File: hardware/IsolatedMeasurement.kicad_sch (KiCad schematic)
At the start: 27 parts, among them IC10 REF196GSZ-REEL, IC4 MCP3561T-E_NC, IC5 ADUM7440ARQZ, P2 AM1LS-0505S-NZ, U3 >

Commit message: board sync and measurments section adjustments
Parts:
- C46: value 1nF -> 100nF
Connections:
- net HV_+3.3V: now also C46.1, IC10.2 (VSS), IC10.3 (~{SLEEP})
- net HV_+5V: no longer names the net of C56.1, C58.2, P2.5 (VOUT+), R12.2, U3.3 (VI)
- net HV_+5V: no longer C46.1, IC10.2 (VSS), IC10.3 (~{SLEEP})
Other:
- note added: "3V REF"
- note added: "Minimal current - 20mA R12 - additional load resistor to cap the current draw"
- note removed: "Minimal current - 20mA R - additional load resistor to cap the current draw"
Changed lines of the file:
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@@
     (stroke (width 0) (type default) (color 0 0 0 0))
   )
-  (text "Minimal current - 20mA\nR - additional load resistor to cap\nthe current draw"
+  (text "Minimal current - 20mA\nR12 - additional load resistor to cap\nthe current draw"
     (at 243.84 50.165 0)
     (effects (font (size 1.27 1.27)) (justify left bottom))
@@
     (effects (font (size 1.27 1.27)) (justify left bottom))
   )
+  (text "3V REF\n" (at 122.555 135.89 0)
+    (effects (font (size 3 3) (thickness 1) bold) (justify left bottom))
+  )
   (text "SPI iso\n" (at 214.63 111.125 0)
     (effects (font (size 5 5) (thickness 1) bold) (justify left bottom))
@@
     (effects (font (size 1.27 1.27)) (justify right bottom))
   )
-  (label "HV_+5V" (at 233.045 62.865 90)
-    (effects (font (size 1.27 1.27)) (justify left bottom))
-  )
   (label "3.3V_REF" (at 60.325 134.62 180)
     (effects (font (size 1.27 1.27)) (justify right bottom))
@@
     (effects (font (size 1.27 1.27)) (justify left bottom))
   )
+  (label "HV_+3.3V" (at 116.205 142.24 90)
+    (effects (font (size 1.27 1.27)) (justify left bottom))
+  )
   (label "HV_+3.3V" (at 264.795 65.405 0)
     (effects (font (size 1.27 1.27)) (justify left bottom))
@@
   )
   (label "SDO" (at 149.86 52.705 0)
-    (effects (font (size 1.27 1.27)) (justify left bottom))
-  )
-  (label "HV_+5V" (at 116.205 142.24 90)
     (effects (font (size 1.27 1.27)) (justify left bottom))
   )
@@
       (effects (font (size 1.27 1.27)) (justify left))
     )
-    (property "Value" "1nF" (id 1) (at 111.125 157.48 90)
-      (effects (font (size 1.27 1.27)) (justify left))
-    )
+    (property "Value" "100nF" (id 1) (at 111.125 157.48 90)
+      (effects (font (size 1.27 1.27)) (justify left))
+    )

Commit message: measurments section changes, sorted components on the board into groups, changed main connector and added seprate for AIRs, added IMD PWM input as well as AIR fault detection
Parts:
- removed U3: >, symbol Regulator_Linear:LM1117-3.3
- added IC11: AP7365-33YRG-13, AP736533YRG13, symbol AP7365-33YRG-13:AP7365-33YRG-13
- C58, C59: value 1uF -> 100nF
- IC10: value REF196GSZ-REEL -> REF193GSZ-REEL
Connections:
- net HV_+3.3V: now also IC11.3 (VO)
- net HV_IN-: now also IC11.1 (GND)
- net V_HV+: now also IC4.4 (CH1); no longer IC4.3 (CH0)
- net V_HV-: now also IC4.3 (CH0); no longer IC4.4 (CH1)
- net at C56.1, C58.2, P2.5 (VOUT+)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: now also IC11.2 (VI)
- net 3.3V_REF renamed 3V_REF
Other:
- note added: "Minimal current - 20mA R - additional load resistor to cap the current draw"
- note added: "V_HV_REF- can be adjusted, default is HV_GND WARNING! USES REF_V! that means high resistance & precision resistors should be used"
- note added: "V_{inmax} = 2,2k / (2,2 k + 4 x 200k) * 600 = ~1,65V I_{max} = 600V / 802,2kOhm = ~0,000747A P_{max} = 0,000747A * 600V = 0,4482W P_{max1R} = 0,000747A * 598,35V = 0,44696745W P_{max4R} = 0,000747A * P_{max1R} / 4 = 0,1117418625W P_{maxR} = ~0,25W????"
- note removed: "Minimal current - 20mA R12 - additional load resistor to cap the current draw"
- note removed: "V_HV_REF- can be adjusted, default is HV_GND"
- note removed: "V_{inmax} = 2,2k / (2,2 k + 4 x 200k) * 600 = ~1,65V I_{max} = 600V / 802,2kOhm = ~0,000747A P_{max} = 0,000747A * 600V = 0,4482W P_{max1R} = 0,000747A * 598,35V = 0,44696745W P_{max4R} = 0,000747A * P_{max1R} / 4 = 0,1117418625W P_{maxR} = ~0,25W???? (i guess)"
- moved on the sheet: R25, R26

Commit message: changed few connectors, finished board HV section and other minor changes
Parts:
- renumbered C23 to C13, C26 to C14, C31 to C17, C32 to C18, C33 to C19, C47 to C20, C49 to C36, C56 to C37, C58 to C38, C59 to C39, C22 to C7, C46 to C9, IC4 to IC2, IC5 to IC3, IC11 to IC6, IC10 to IC9, L7 to L2, L6 to L5, P2 to P1, R2 to R1, R12 to R11, R25 to R20, R26 to R21, R4 to R3, R6 to R5, R8 to R7, R10 to R9
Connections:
- net SCK: now also IC3.13 (VOB); no longer IC2.12 (SCK), IC3.12 (VOC), IC3.5 (VIC)
- net SDI: now also IC3.12 (VOC); no longer IC2.13 (SDI), IC3.13 (VOB), IC3.4 (VIB)
- net SDO: now also IC3.11 (VOD); no longer IC2.14 (SDO), IC3.14 (VOA), IC3.3 (VIA)
- net ~{CS}: now also IC3.14 (VOA); no longer IC2.11 (~{CS}), IC3.11 (VOD), IC3.6 (VID)
- new net HV_SCK: IC2.12 (SCK), IC3.4 (VIB)
- new net HV_SDI: IC2.13 (SDI), IC3.5 (VIC)
- new net HV_SDO: IC2.14 (SDO), IC3.6 (VID)
- new net HV_~{CS}: IC2.11 (~{CS}), IC3.3 (VIA)

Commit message: board sync
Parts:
- R10: renamed from R9; value 2,2k -> 4k; footprint Resistor_SMD:R_0603_1608Metric -> Resistor_SMD:R_1206_3216Metric
- R2: renamed from R1; footprint Resistor_SMD:R_0603_1608Metric -> Resistor_SMD:R_1206_3216Metric; Mouser Part Number (none) -> 754-RGV3216P-2003BT1
- R4: renamed from R3; footprint Resistor_SMD:R_0603_1608Metric -> Resistor_SMD:R_1206_3216Metric; Mouser Part Number (none) -> 754-RGV3216P-2003BT1
- R6: renamed from R5; footprint Resistor_SMD:R_0603_1608Metric -> Resistor_SMD:R_1206_3216Metric; Mouser Part Number (none) -> 754-RGV3216P-2003BT1
- R8: renamed from R7; footprint Resistor_SMD:R_0603_1608Metric -> Resistor_SMD:R_1206_3216Metric; Mouser Part Number (none) -> 754-RGV3216P-2003BT1
- renumbered C7 to C22, C13 to C23, C14 to C26, C17 to C31, C18 to C32, C19 to C33, C9 to C46, C20 to C47, C36 to C49, C37 to C56, C38 to C58, C39 to C59, IC9 to IC10, IC6 to IC11, IC2 to IC4, IC3 to IC5, L5 to L6, L2 to L7, P1 to P2, R11 to R12, R20 to R25, R21 to R26
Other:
- note added: "V_{max_mes} = 3V 3V = 588V * x / ( 800 000 + x ) 585x = 2'400'000 x = 4102,56 Ohm R = 4kOhm"
- note removed: "V_{inmax} = 2,2k / (2,2 k + 4 x 200k) * 600 = ~1,65V I_{max} = 600V / 802,2kOhm = ~0,000747A P_{max} = 0,000747A * 600V = 0,4482W P_{max1R} = 0,000747A * 598,35V = 0,44696745W P_{max4R} = 0,000747A * P_{max1R} / 4 = 0,1117418625W P_{maxR} = ~0,25W????"

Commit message: remake in progress
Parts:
- renumbered C23 to C13, C26 to C14, C31 to C17, C32 to C18, C33 to C19, C47 to C20, C49 to C36, C56 to C37, C58 to C38, C59 to C39, C22 to C7, C46 to C9, IC4 to IC2, IC5 to IC3, IC11 to IC6, IC10 to IC9, L7 to L2, L6 to L5, P2 to P1, R2 to R1, R12 to R11, R25 to R20, R26 to R21, R4 to R3, R6 to R5, R8 to R7, R10 to R9

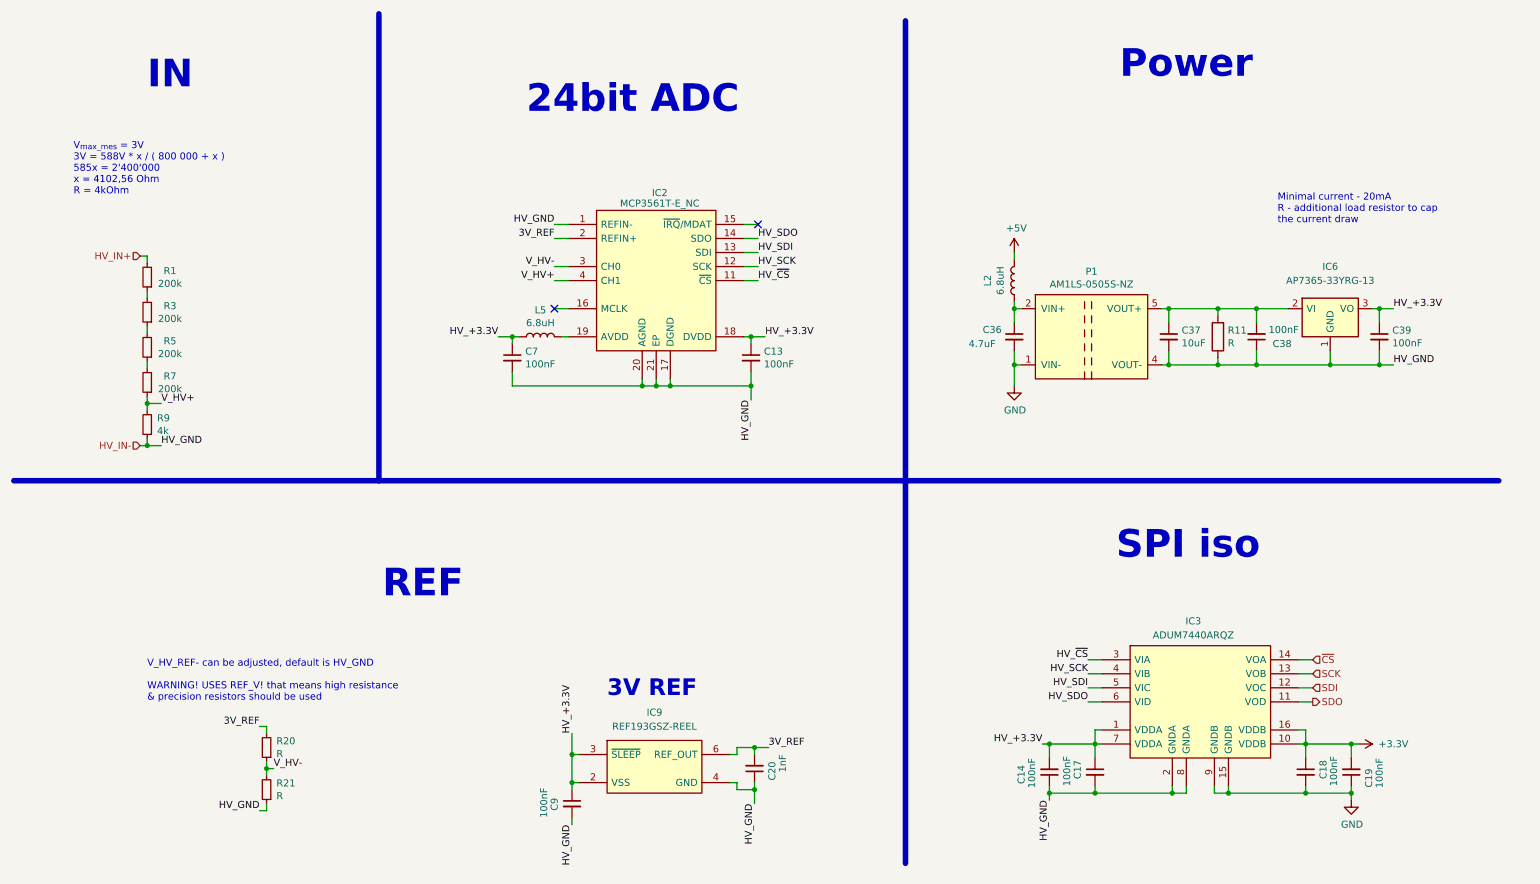
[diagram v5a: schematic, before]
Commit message: major changes: conn, fans, inputs and others
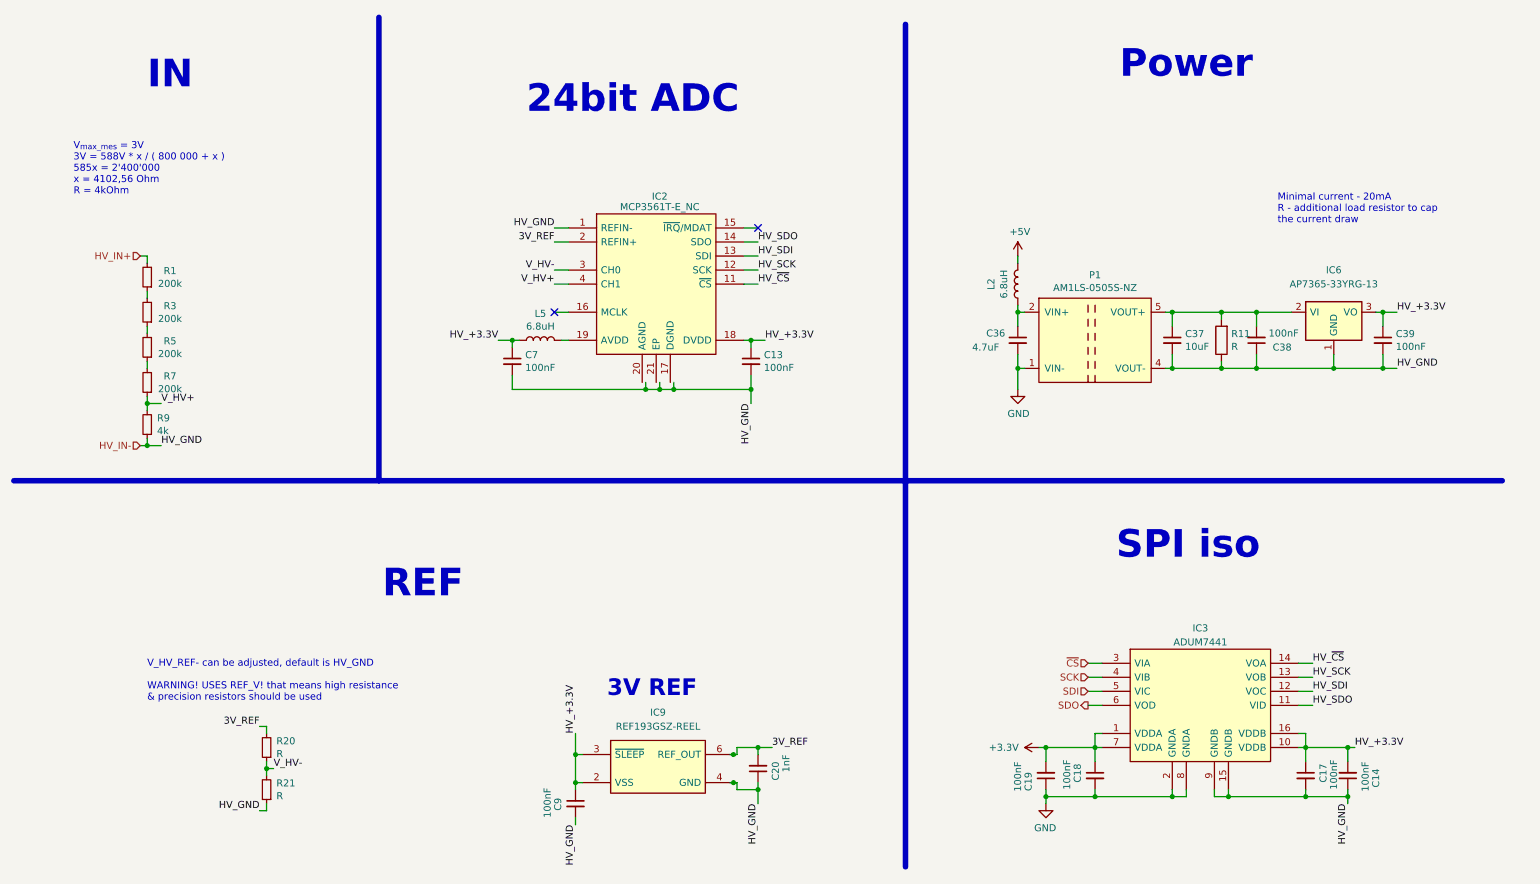
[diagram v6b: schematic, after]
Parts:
- IC3: value ADUM7440ARQZ -> ADUM7441
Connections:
- net +3V3: now also IC3.1 (VDDA), IC3.7 (VDDA); no longer IC3.10 (VDDB), IC3.16 (VDDB)
- net GND: now also IC3.2 (GNDA), IC3.8 (GNDA); no longer IC3.15 (GNDB), IC3.9 (GNDB)
- net HV_+3.3V: now also IC3.10 (VDDB), IC3.16 (VDDB); no longer IC3.1 (VDDA), IC3.7 (VDDA)
- net HV_IN-: now also IC3.15 (GNDB), IC3.9 (GNDB); no longer IC2.17 (DGND), IC2.20 (AGND), IC2.21 (EP), IC3.2 (GNDA), IC3.8 (GNDA)
- net HV_SCK: now also IC3.13 (VOB); no longer IC3.4 (VIB)
- net HV_SDI: now also IC3.12 (VOC); no longer IC3.5 (VIC)
- net HV_SDO: now also IC3.11 (VID); no longer IC3.6 (VID)
- net HV_~{CS}: now also IC3.14 (VOA); no longer IC3.3 (VIA)
- net SCK: now also IC3.4 (VIB); no longer IC3.13 (VOB)
- net SDI: now also IC3.5 (VIC); no longer IC3.12 (VOC)
- net SDO: now also IC3.6 (VOD); no longer IC3.11 (VOD)
- net ~{CS}: now also IC3.3 (VIA); no longer IC3.14 (VOA)
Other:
- moved on the sheet: C13, C14, C17, C18, C19, C20, C36, C37, C38, C39, C7, C9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

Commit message: done
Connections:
- net HV_IN-: now also IC2.17 (DGND), IC2.20 (AGND), IC2.21 (EP)
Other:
- moved on the sheet: C13, C7, IC2, L5

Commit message: WęGoRz AfTeR rEvIeW cOmMiT
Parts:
- renumbered R1 to R60
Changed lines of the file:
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@@
   (symbol (lib_id "Device:R_Small") (at 39.37 59.69 180) (unit 1)
     (in_bom yes) (on_board yes) (dnp no)
-    (property "Reference" "R1" (at 43.4975 58.5597 0)
+    (property "Reference" "R60" (at 43.4975 58.5597 0)
       (effects (font (size 1.27 1.27)))
     )
@@
       (project "PUTM_EV_BMS_HV_Master_2021"
         (path "/b456cffc-d9d7-4c91-91f2-36ec9a65dd1b/e61cc821-5479-4c04-b5ab-4a32f17b4f03/d2e30d51-b8f8-4bbd-bb5a-76e0eb119260"
-          (reference "R1") (unit 1)
+          (reference "R60") (unit 1)
         )
         (path "/b456cffc-d9d7-4c91-91f2-36ec9a65dd1b/e61cc821-5479-4c04-b5ab-4a32f17b4f03/6b03d8c8-5f6c-4244-9202-23821031eb5e"
